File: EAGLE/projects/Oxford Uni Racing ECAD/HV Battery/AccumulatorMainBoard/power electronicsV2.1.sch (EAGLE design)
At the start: 93 parts, among them IC1 4043D, IC2 SE555D, IC3 4011D, IC5 4043D, IC6 4011D, IC7 4011D, IC8 4011D, IC9 4011D, K1 T9AS1D12-48=T9A, K2 T9AS5D12-12=T9A, K3 T9AS1D12-48=T9A, K4 T9AS1D12-48=T9A, K5 T9AS1D12-48=T9A, Q1 BSS138, Q2 BSS138, Q3 BSS138, Q4 BSS138, Q5 BSS138, X1 CAN 1, X2 CAN 2

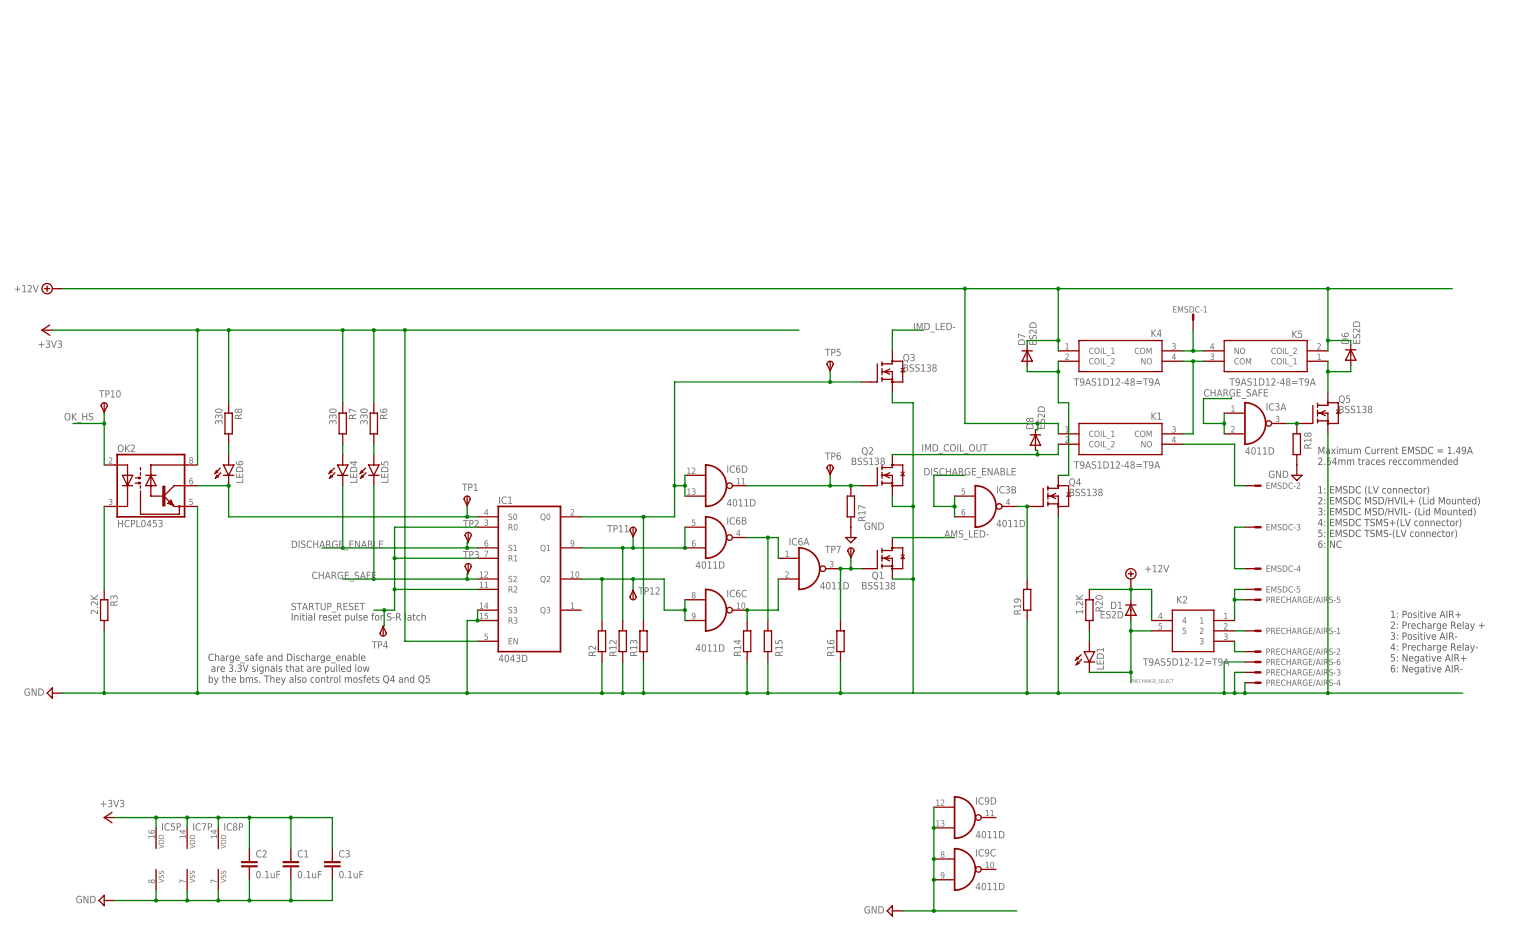
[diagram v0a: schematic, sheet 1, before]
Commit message: Update to main accumulator board
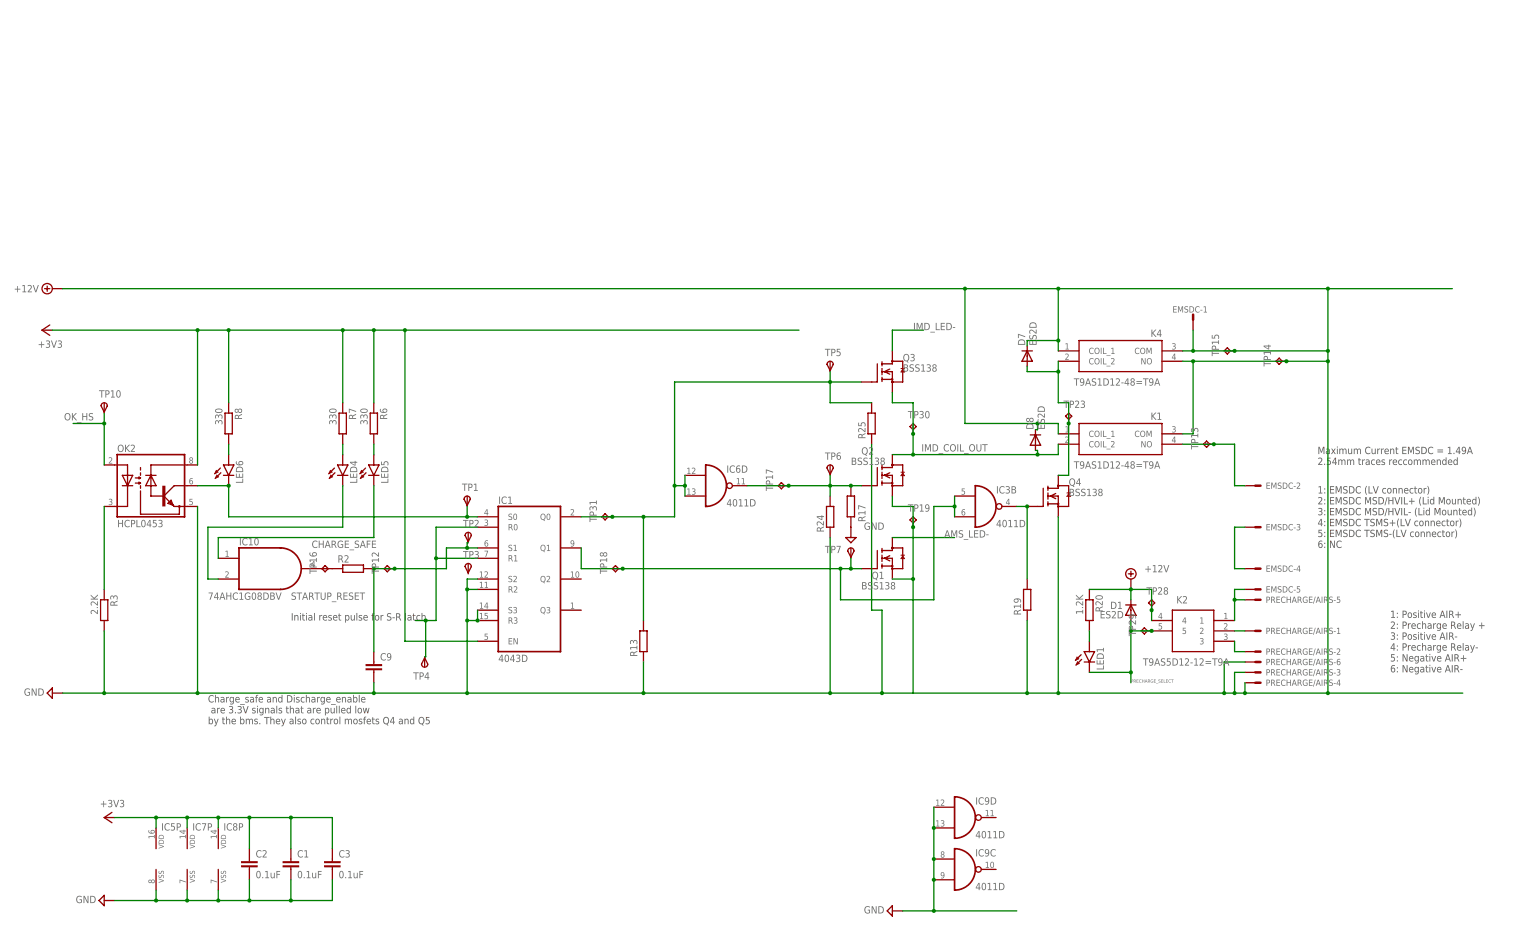
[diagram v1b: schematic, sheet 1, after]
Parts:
- removed D6: ES2D, diode:ES2D
- removed K5: T9AS1D12-48=T9A, SamacSys_Parts:T9AS1D12-48=T9A
- removed Q5: BSS138, m-pad-2.1:BSS138
- removed R12, R14, R15, R16, R18: (no value), rcl:R-EU_R0805
- removed TP11: TPSTP11R, testpad:TPSTP11R
- added C9: (no value), rcl:C-EUC0805K
- added IC10: 74AHC1G08DBV, 74xx-little-us:74AHC1G08DBV
- added R24, R25: (no value), rcl:R-EU_R0805
- added TP13, TP14, TP15, TP16, TP17, TP18, TP19, TP23, TP28, TP29, TP30, TP31: TPTP17R, testpad:TPTP17R
- TP12: value TPSTP11R -> TPTP17R; device testpad:TPSTP11R -> testpad:TPTP17R
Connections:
- removed net EMSDC_IMD+: K1.COM, K4.NO, K5.COM
- removed net N$18: IC3A.O, Q5.G, R18.2
- removed net N$20: IC6A.I1, IC6C.O, R14.2
- removed net N$21: IC6A.O, Q1.G, R16.2, TP7.PP
- removed net N$29: IC6C.I0, IC6C.I1
- removed net N$37: IC6D.O, Q2.G, R17.2, TP6.PP
- removed net N$6: D7.A, K4.COIL_2, Q4.D
- net +12V: now also C9.2, EMSDC-1.S, IC1A.R2, IC1A.R3, IC1A.S2, IC1A.S3, K1.COM, K4.COM, K4.NO, OK2.GND, PRECHARGE/AIRS-3.S, PRECHARGE/AIRS-4.S, PRECHARGE/AIRS-6.S, Q1.S, Q2.S, Q4.S, R13.1, R19.1, R24.1, R25.1, R3.2, TP14.TP, TP15.TP, TP19.TP, TP28.TP; no longer D6.C, K5.COIL_2
- net CHARGE_SAFE: now also IC10A.I0; no longer IC1A.S2, IC3A.I0, IC3A.I1, TP3.PP
- net DISCHARGE_ENABLE: now also IC1A.Q1, Q1.G, TP18.TP, TP7.PP; no longer IC1A.S1, LED4.C, TP2.PP
- net GND: no longer IC1A.R3, IC1A.S3, OK2.GND, PRECHARGE/AIRS-3.S, PRECHARGE/AIRS-4.S, PRECHARGE/AIRS-6.S, Q1.S, Q2.S, Q3.S, Q4.S, Q5.S, R12.1, R13.1, R14.1, R15.1, R16.1, R18.1, R19.1, R2.1, R3.2
- net IMD_COIL_OUT: now also Q3.S, TP30.TP
- net N$1: now also R2.1, TP16.TP; no longer EMSDC-1.S, K4.COM, K5.NO
- net N$10: now also C9.1, IC1A.S1, R2.2, TP12.TP, TP2.PP; no longer IC1A.Q1, IC6B.I0, IC6B.I1, R12.2, TP11.PP
- net N$13: now also IC10A.I1, LED4.C; no longer IC1A.Q2, R2.2, TP12.PP
- net N$14: now also EMSDC-2.S, K1.NO, TP13.TP; no longer IC6A.I0, IC6B.O, R15.2
- net N$15: now also D7.A, K4.COIL_2, Q4.D, TP23.TP; no longer EMSDC-2.S, K1.NO
- net N$8: now also IC6D.O, Q2.G, R17.2, R24.2, TP17.TP, TP6.PP; no longer IC1A.Q0, Q3.G, R13.2, TP5.PP
- net N$9: now also IC1A.Q0, Q3.G, R13.2, R25.2, TP31.TP, TP5.PP; no longer D6.A, K5.COIL_1, Q5.D
- net PRECHARGE_SELECT: now also TP29.TP
- net STARTUP_RESET: no longer IC1A.R2
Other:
- moved on the sheet: R2, TP4

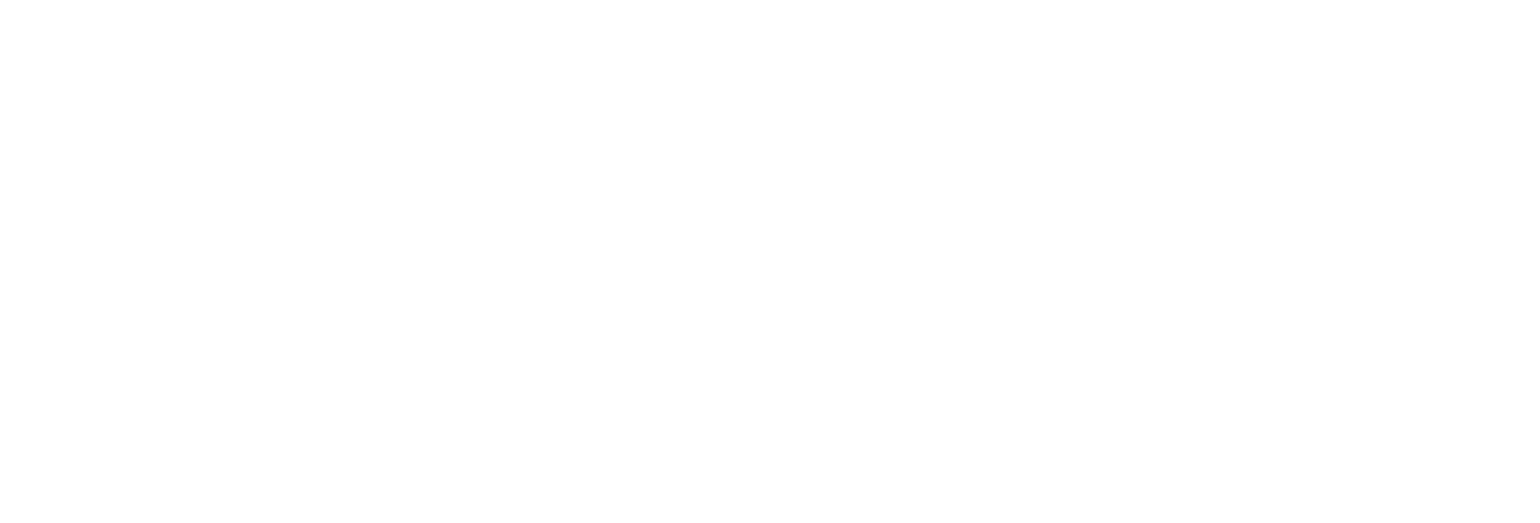
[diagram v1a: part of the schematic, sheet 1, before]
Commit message: New D-sub connectors
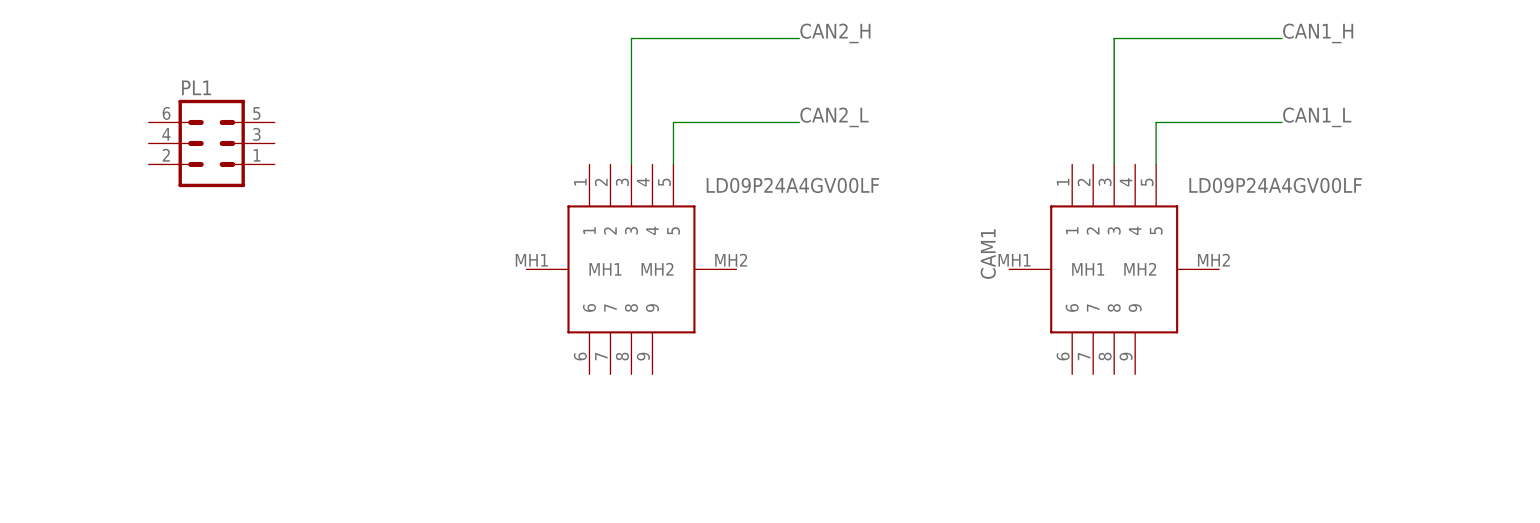
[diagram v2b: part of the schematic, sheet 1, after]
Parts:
- added CAM1, CAM2: LD09P24A4GV00LF, LD09P24A4GV00LF:LD09P24A4GV00LF
- added PL1: (no value), con-harting-v:06V
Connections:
- net CAN1_H: now also CAM1.3
- net CAN1_L: now also CAM1.5
- net CAN2_H: now also CAM2.3
- net CAN2_L: now also CAM2.5
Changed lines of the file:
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@@
 <part name="TP30" library="testpad" library_urn="urn:adsk.eagle:library:385" deviceset="TP" device="TP17R" package3d_urn="urn:adsk.eagle:package:27971/1"/>
 <part name="TP31" library="testpad" library_urn="urn:adsk.eagle:library:385" deviceset="TP" device="TP17R" package3d_urn="urn:adsk.eagle:package:27971/1"/>
+<part name="CAM1" library="LD09P24A4GV00LF" deviceset="LD09P24A4GV00LF" device=""/>
+<part name="CAM2" library="LD09P24A4GV00LF" deviceset="LD09P24A4GV00LF" device=""/>
+<part name="PL1" library="con-harting-v" library_urn="urn:adsk.eagle:library:150" deviceset="06V" device="" package3d_urn="urn:adsk.eagle:package:7042/1"/>
 </parts>
 <sheets>
@@
 <attribute name="NAME" x="62.23" y="44.45" size="1.778" layer="95" rot="R90"/>
 <attribute name="TP_SIGNAL_NAME" x="64.77" y="46.99" size="1.778" layer="97" rot="R90"/>
+</instance>
+<instance part="CAM1" gate="G$1" x="220.98" y="139.7" smashed="yes">
+<attribute name="NAME" x="218.44" y="138.43" size="1.778" layer="95" rot="R90" align="center-left"/>
+<attribute name="VALUE" x="242.57" y="149.86" size="1.778" layer="96" align="center-left"/>
+</instance>
+<instance part="CAM2" gate="G$1" x="162.56" y="139.7" smashed="yes">
+<attribute name="VALUE" x="184.15" y="149.86" size="1.778" layer="96" align="center-left"/>
+</instance>
+<instance part="PL1" gate="G$1" x="124.46" y="154.94" smashed="yes">
+<attribute name="VALUE" x="120.65" y="147.32" size="1.778" layer="96"/>
+<attribute name="NAME" x="120.65" y="160.782" size="1.778" layer="95"/>
 </instance>
 </instances>
@@
 </segment>
 </net>
+<net name="CAN1_L" class="0">
+<segment>
+<pinref part="CAM1" gate="G$1" pin="5"/>
+<wire x1="238.76" y1="152.4" x2="238.76" y2="157.48" width="0.1524" layer="91"/>
+<wire x1="238.76" y1="157.48" x2="254" y2="157.48" width="0.1524" layer="91"/>
+<label x="254" y="157.48" size="1.778" layer="95"/>
+</segment>
+</net>
+<net name="CAN1_H" class="0">
+<segment>
+<pinref part="CAM1" gate="G$1" pin="3"/>
+<wire x1="233.68" y1="152.4" x2="233.68" y2="167.64" width="0.1524" layer="91"/>
+<wire x1="233.68" y1="167.64" x2="254" y2="167.64" width="0.1524" layer="91"/>
+<label x="254" y="167.64" size="1.778" layer="95"/>
+</segment>
+</net>
+<net name="CAN2_L" class="0">
+<segment>
+<pinref part="CAM2" gate="G$1" pin="5"/>
+<wire x1="180.34" y1="152.4" x2="180.34" y2="157.48" width="0.1524" layer="91"/>
+<wire x1="180.34" y1="157.48" x2="195.58" y2="157.48" width="0.1524" layer="91"/>
+<label x="195.58" y="157.48" size="1.778" layer="95"/>
+</segment>
+</net>
+<net name="CAN2_H" class="0">
+<segment>
+<pinref part="CAM2" gate="G$1" pin="3"/>
+<wire x1="175.26" y1="152.4" x2="175.26" y2="167.64" width="0.1524" layer="91"/>
+<wire x1="175.26" y1="167.64" x2="195.58" y2="167.64" width="0.1524" layer="91"/>
+<label x="195.58" y="167.64" size="1.778" layer="95"/>
+</segment>
+</net>

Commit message: main board
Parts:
- renumbered CAM1 to CAN1, CAM2 to CAN2
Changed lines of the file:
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@@
 <part name="TP30" library="testpad" library_urn="urn:adsk.eagle:library:385" deviceset="TP" device="TP17R" package3d_urn="urn:adsk.eagle:package:27971/1"/>
 <part name="TP31" library="testpad" library_urn="urn:adsk.eagle:library:385" deviceset="TP" device="TP17R" package3d_urn="urn:adsk.eagle:package:27971/1"/>
-<part name="CAM1" library="LD09P24A4GV00LF" deviceset="LD09P24A4GV00LF" device=""/>
-<part name="CAM2" library="LD09P24A4GV00LF" deviceset="LD09P24A4GV00LF" device=""/>
+<part name="CAN1" library="LD09P24A4GV00LF" deviceset="LD09P24A4GV00LF" device=""/>
+<part name="CAN2" library="LD09P24A4GV00LF" deviceset="LD09P24A4GV00LF" device=""/>
 <part name="PL1" library="con-harting-v" library_urn="urn:adsk.eagle:library:150" deviceset="06V" device="" package3d_urn="urn:adsk.eagle:package:7042/1"/>
 </parts>
@@
 <attribute name="TP_SIGNAL_NAME" x="64.77" y="46.99" size="1.778" layer="97" rot="R90"/>
 </instance>
-<instance part="CAM1" gate="G$1" x="220.98" y="139.7" smashed="yes">
+<instance part="CAN1" gate="G$1" x="220.98" y="139.7" smashed="yes">
 <attribute name="NAME" x="218.44" y="138.43" size="1.778" layer="95" rot="R90" align="center-left"/>
 <attribute name="VALUE" x="242.57" y="149.86" size="1.778" layer="96" align="center-left"/>
 </instance>
-<instance part="CAM2" gate="G$1" x="162.56" y="139.7" smashed="yes">
+<instance part="CAN2" gate="G$1" x="162.56" y="139.7" smashed="yes">
 <attribute name="VALUE" x="184.15" y="149.86" size="1.778" layer="96" align="center-left"/>
 </instance>
@@
 <net name="CAN1_L" class="0">
 <segment>
-<pinref part="CAM1" gate="G$1" pin="5"/>
+<pinref part="CAN1" gate="G$1" pin="5"/>
 <wire x1="238.76" y1="152.4" x2="238.76" y2="157.48" width="0.1524" layer="91"/>
 <wire x1="238.76" y1="157.48" x2="254" y2="157.48" width="0.1524" layer="91"/>
@@
 <net name="CAN1_H" class="0">
 <segment>
-<pinref part="CAM1" gate="G$1" pin="3"/>
+<pinref part="CAN1" gate="G$1" pin="3"/>
 <wire x1="233.68" y1="152.4" x2="233.68" y2="167.64" width="0.1524" layer="91"/>
 <wire x1="233.68" y1="167.64" x2="254" y2="167.64" width="0.1524" layer="91"/>
@@
 <net name="CAN2_L" class="0">
 <segment>
-<pinref part="CAM2" gate="G$1" pin="5"/>
+<pinref part="CAN2" gate="G$1" pin="5"/>
 <wire x1="180.34" y1="152.4" x2="180.34" y2="157.48" width="0.1524" layer="91"/>
 <wire x1="180.34" y1="157.48" x2="195.58" y2="157.48" width="0.1524" layer="91"/>
@@
 <net name="CAN2_H" class="0">
 <segment>
-<pinref part="CAM2" gate="G$1" pin="3"/>
+<pinref part="CAN2" gate="G$1" pin="3"/>
 <wire x1="175.26" y1="152.4" x2="175.26" y2="167.64" width="0.1524" layer="91"/>
 <wire x1="175.26" y1="167.64" x2="195.58" y2="167.64" width="0.1524" layer="91"/>
